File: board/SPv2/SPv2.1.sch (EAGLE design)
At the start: 35 parts, among them IC1 S34ML0XG1, IC2 F5508, IC4 74LS14D, Q1 12MHz

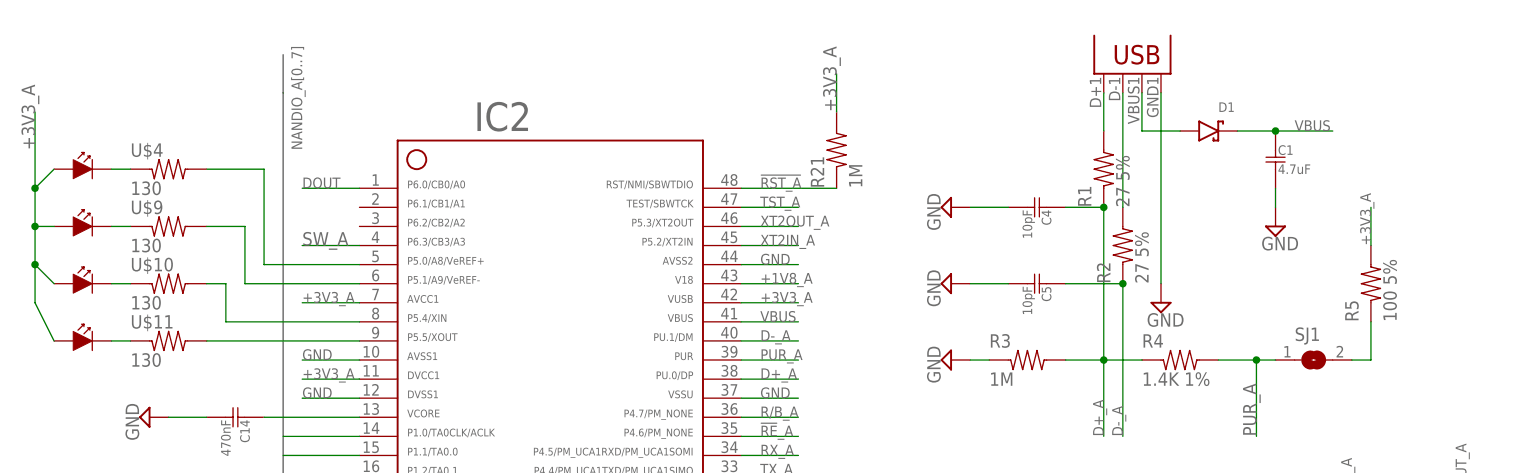
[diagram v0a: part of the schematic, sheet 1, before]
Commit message: updated part sizes and numbering
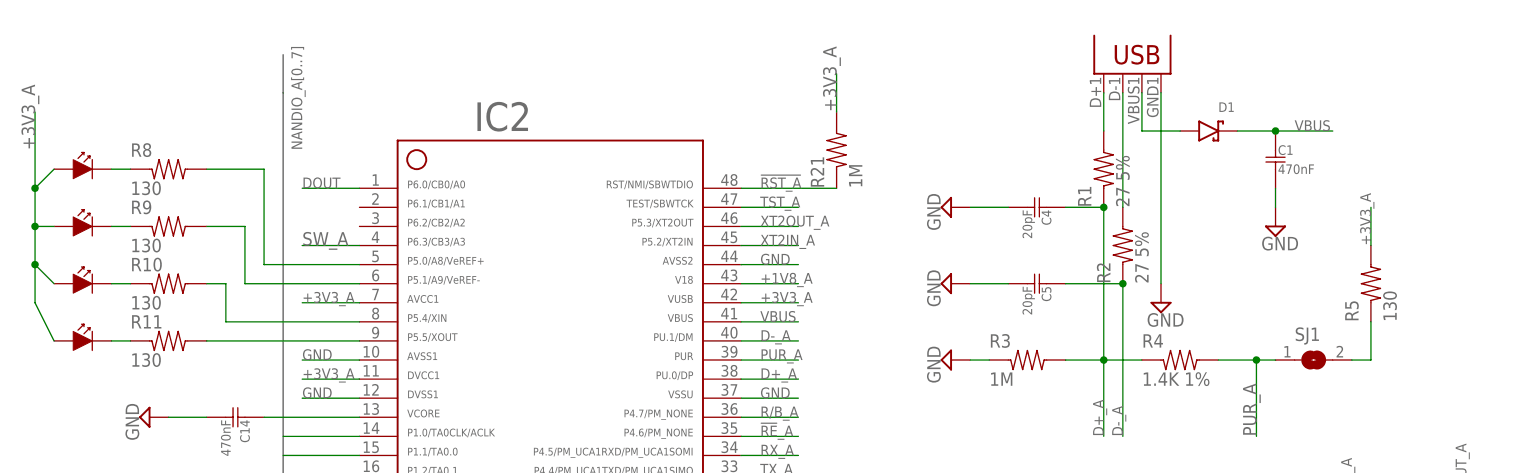
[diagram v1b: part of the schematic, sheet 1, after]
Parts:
- C1: value 4.7uF -> 470nF
- C4, C5: value 10pF -> 20pF
- R5: value 100 5% -> 130
- renumbered U$10 to R10, U$11 to R11, U$4 to R8, U$9 to R9
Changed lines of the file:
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@@
 <?xml version="1.0" encoding="utf-8"?>
 <!DOCTYPE eagle SYSTEM "eagle.dtd">
-<eagle version="6.5.0">
+<eagle version="7.1.0">
 <drawing>
 <settings>
@@
 <part name="SUPPLY1" library="supply2" deviceset="GND" device=""/>
 <part name="JP1" library="Passives" deviceset="USB" device="A-SMD-MALE" value="USBA-SMD-MALE"/>
-<part name="C1" library="Passives" deviceset="C" device="0805" value="4.7uF"/>
+<part name="C1" library="Passives" deviceset="C" device="0805" value="470nF"/>
 <part name="C2" library="Passives" deviceset="C" device="0805" value="220nF"/>
 <part name="C3" library="Passives" deviceset="C" device="0805" value="220nF"/>
-<part name="C4" library="Passives" deviceset="C" device="0805" value="10pF"/>
-<part name="C5" library="Passives" deviceset="C" device="0805" value="10pF"/>
+<part name="C4" library="Passives" deviceset="C" device="0805" value="20pF"/>
+<part name="C5" library="Passives" deviceset="C" device="0805" value="20pF"/>
 <part name="C6" library="Passives" deviceset="C" device="0805" value="20pF"/>
 <part name="C7" library="Passives" deviceset="C" device="0805" value="20pF"/>
@@
 <part name="SUPPLY10" library="supply2" deviceset="GND" device=""/>
 <part name="R4" library="Passives" deviceset="R" device="0805" value="1.4K 1%"/>
-<part name="R5" library="Passives" deviceset="R" device="0805" value="100 5%"/>
+<part name="R5" library="Passives" deviceset="R" device="0805" value="130"/>
 <part name="C14" library="Passives" deviceset="C" device="0805" value="470nF"/>
 <part name="SUPPLY18" library="supply2" deviceset="GND" device=""/>
@@
 <part name="U$7" library="Passives" deviceset="LED" device=""/>
 <part name="U$8" library="Passives" deviceset="LED" device=""/>
-<part name="U$4" library="Passives" deviceset="R" device="0805" value="130"/>
-<part name="U$9" library="Passives" deviceset="R" device="0805" value="130"/>
-<part name="U$10" library="Passives" deviceset="R" device="0805" value="130"/>
-<part name="U$11" library="Passives" deviceset="R" device="0805" value="130"/>
+<part name="R8" library="Passives" deviceset="R" device="0805" value="130"/>
+<part name="R9" library="Passives" deviceset="R" device="0805" value="130"/>
+<part name="R10" library="Passives" deviceset="R" device="0805" value="130"/>
+<part name="R11" library="Passives" deviceset="R" device="0805" value="130"/>
 <part name="D1" library="Passives" deviceset="D-SCHOTTKY" device=""/>
 <part name="IC4" library="74xx-us" deviceset="74*14" device="D" technology="LS"/>
@@
 <instance part="U$7" gate="G$1" x="-12.7" y="104.14"/>
 <instance part="U$8" gate="G$1" x="-12.7" y="96.52"/>
-<instance part="U$4" gate="G$1" x="-2.54" y="119.38"/>
-<instance part="U$9" gate="G$1" x="-2.54" y="111.76"/>
-<instance part="U$10" gate="G$1" x="-2.54" y="104.14"/>
-<instance part="U$11" gate="G$1" x="-2.54" y="96.52"/>
+<instance part="R8" gate="G$1" x="-2.54" y="119.38"/>
+<instance part="R9" gate="G$1" x="-2.54" y="111.76"/>
+<instance part="R10" gate="G$1" x="-2.54" y="104.14"/>
+<instance part="R11" gate="G$1" x="-2.54" y="96.52"/>
 <instance part="D1" gate="G$1" x="137.16" y="124.46"/>
 <instance part="SJ1" gate="1" x="149.86" y="93.98"/>
@@
 <segment>
 <pinref part="U$7" gate="G$1" pin="CATHODE"/>
-<pinref part="U$10" gate="G$1" pin="1"/>
+<pinref part="R10" gate="G$1" pin="1"/>
 <wire x1="-10.16" y1="104.14" x2="-7.62" y2="104.14" width="0.1524" layer="91"/>
 </segment>
@@
 <segment>
 <pinref part="U$6" gate="G$1" pin="CATHODE"/>
-<pinref part="U$9" gate="G$1" pin="1"/>
+<pinref part="R9" gate="G$1" pin="1"/>
 <wire x1="-10.16" y1="111.76" x2="-7.62" y2="111.76" width="0.1524" layer="91"/>
 </segment>
@@
 <segment>
 <pinref part="U$5" gate="G$1" pin="CATHODE"/>
-<pinref part="U$4" gate="G$1" pin="1"/>
+<pinref part="R8" gate="G$1" pin="1"/>
 <wire x1="-10.16" y1="119.38" x2="-7.62" y2="119.38" width="0.1524" layer="91"/>
 </segment>
@@
 <segment>
 <pinref part="U$8" gate="G$1" pin="CATHODE"/>
-<pinref part="U$11" gate="G$1" pin="1"/>
+<pinref part="R11" gate="G$1" pin="1"/>
 <wire x1="-10.16" y1="96.52" x2="-7.62" y2="96.52" width="0.1524" layer="91"/>
 </segment>
@@
 <net name="N$19" class="0">
 <segment>
-<pinref part="U$11" gate="G$1" pin="2"/>
+<pinref part="R11" gate="G$1" pin="2"/>
 <pinref part="IC2" gate="G$1" pin="9"/>
 <wire x1="2.54" y1="96.52" x2="22.86" y2="96.52" width="0.1524" layer="91"/>
@@
 <wire x1="22.86" y1="99.06" x2="5.08" y2="99.06" width="0.1524" layer="91"/>
 <wire x1="5.08" y1="99.06" x2="5.08" y2="104.14" width="0.1524" layer="91"/>
-<pinref part="U$10" gate="G$1" pin="2"/>
+<pinref part="R10" gate="G$1" pin="2"/>
 <wire x1="5.08" y1="104.14" x2="2.54" y2="104.14" width="0.1524" layer="91"/>
 </segment>
@@
 <net name="N$27" class="0">
 <segment>
-<pinref part="U$9" gate="G$1" pin="2"/>
+<pinref part="R9" gate="G$1" pin="2"/>
 <wire x1="2.54" y1="111.76" x2="7.62" y2="111.76" width="0.1524" layer="91"/>
 <wire x1="7.62" y1="111.76" x2="7.62" y2="104.14" width="0.1524" layer="91"/>
@@
 <net name="N$28" class="0">
 <segment>
-<pinref part="U$4" gate="G$1" pin="2"/>
+<pinref part="R8" gate="G$1" pin="2"/>
 <wire x1="2.54" y1="119.38" x2="10.16" y2="119.38" width="0.1524" layer="91"/>
 <wire x1="10.16" y1="119.38" x2="10.16" y2="106.68" width="0.1524" layer="91"/>
